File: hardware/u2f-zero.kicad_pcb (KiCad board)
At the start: 2 copper layers, 40.5 x 14.5 mm, 16 parts, among them SW1 SW_PUSH

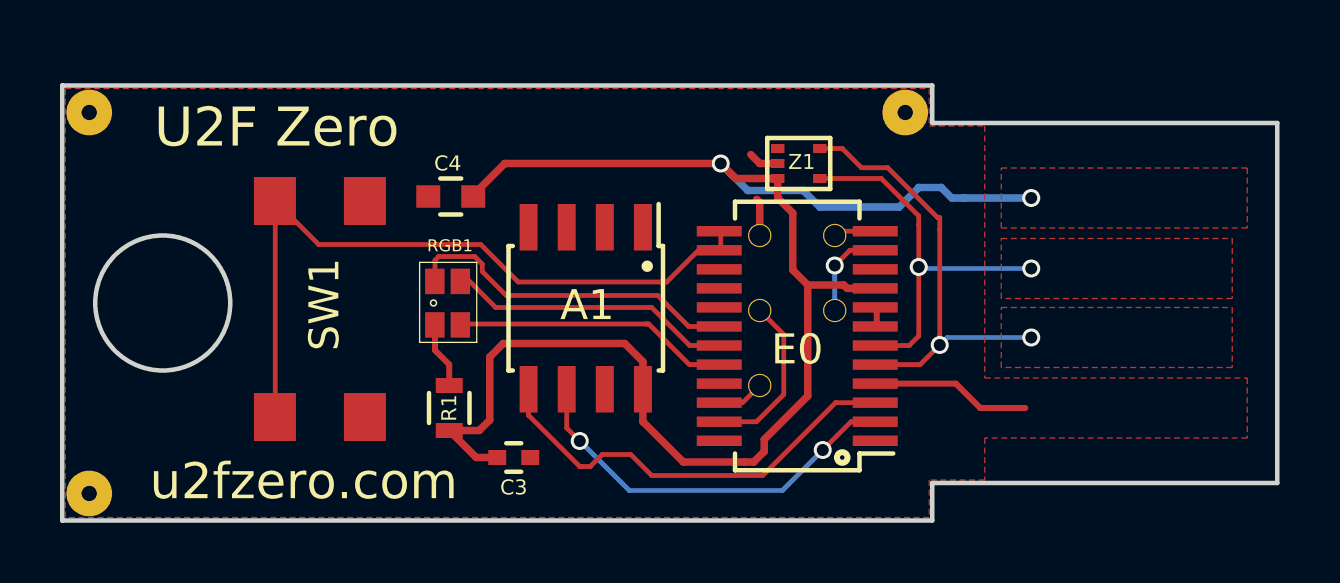
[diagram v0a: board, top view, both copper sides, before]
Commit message: changed usb connector from pcb connector to surface soldered connector
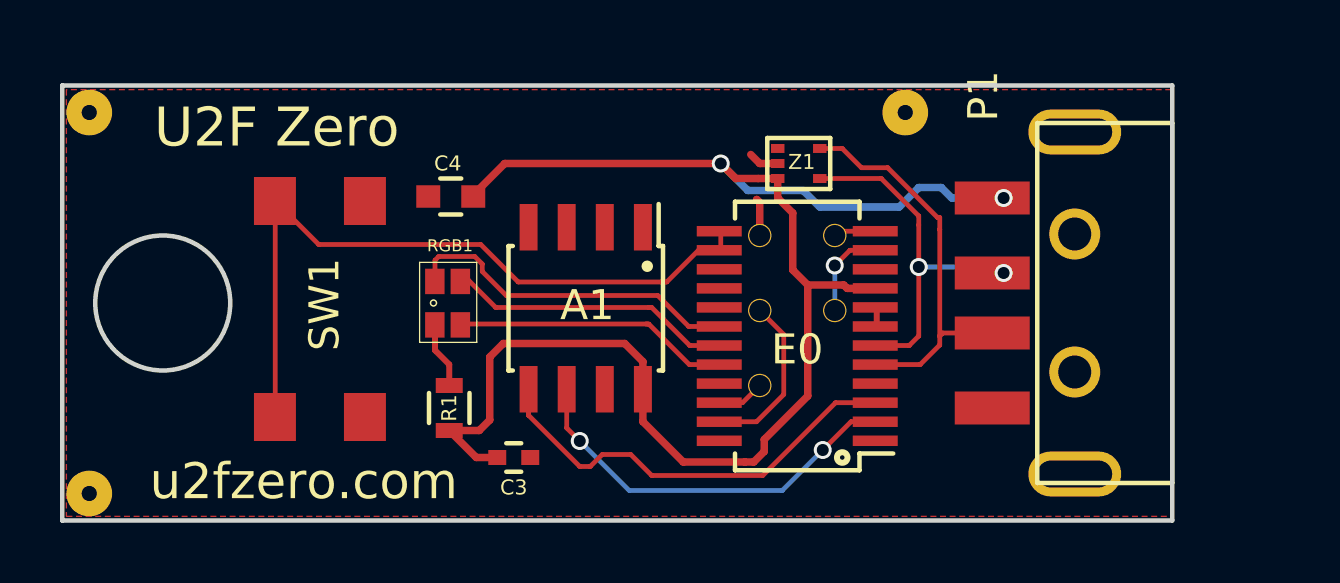
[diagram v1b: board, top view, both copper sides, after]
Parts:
- added P1: USB_A, footprints:USB_A_CON, F.Cu at (72.2, 36.2)
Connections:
- A1 pad 1: Net-(A1-Pad1) -> (no net)
- A1 pad 2: Net-(A1-Pad2) -> (no net)
- A1 pad 3: Net-(A1-Pad3) -> (no net)
- A1 pad 7: Net-(A1-Pad7) -> (no net)
- E0 pad 1: Net-(E0-Pad1) -> (no net)
- E0 pad 10: Net-(E0-Pad10) -> (no net)
- E0 pad 15: Net-(E0-Pad15) -> (no net)
- E0 pad 16: Net-(E0-Pad16) -> (no net)
- E0 pad 17: Net-(E0-Pad17) -> (no net)
- E0 pad 21: Net-(E0-Pad21) -> (no net)
- E0 pad 24: Net-(E0-Pad24) -> (no net)
- Z1 pad 1: Net-(Z1-Pad1) -> (no net)
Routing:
- net GND: track 7.69 -> 2.41 mm
- net /HD+: track 14.7 -> 13.4 mm, vias 2 -> 0
- net /+5V: track 52.5 -> 51.6 mm
- net /HD-: track 13.1 -> 12.3 mm
- removed copper zone on F.Cu, net /+5V
- removed copper zone on F.Cu, net /HD+
- removed copper zone on F.Cu, net /HD-
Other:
- board size 40.5 x 14.5 mm -> 37 x 14.5 mm
